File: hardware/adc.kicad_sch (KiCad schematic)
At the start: 6 parts, among them U2 AD8603

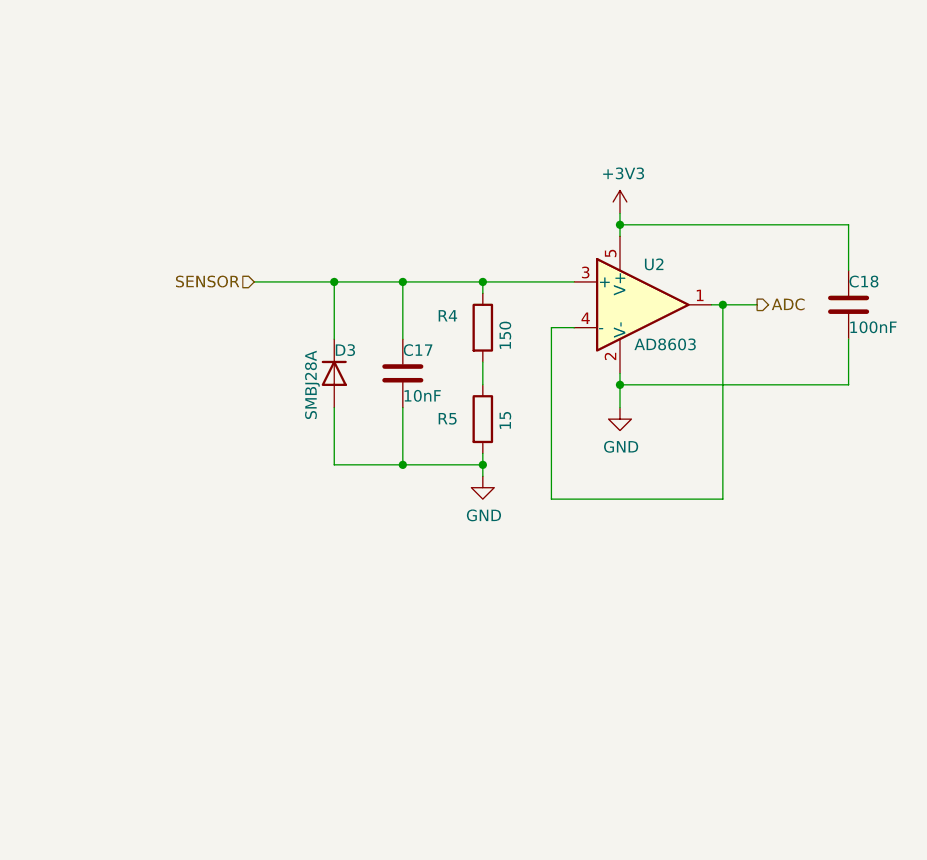
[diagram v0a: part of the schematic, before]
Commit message: MCU BOOT0 mistake fixed
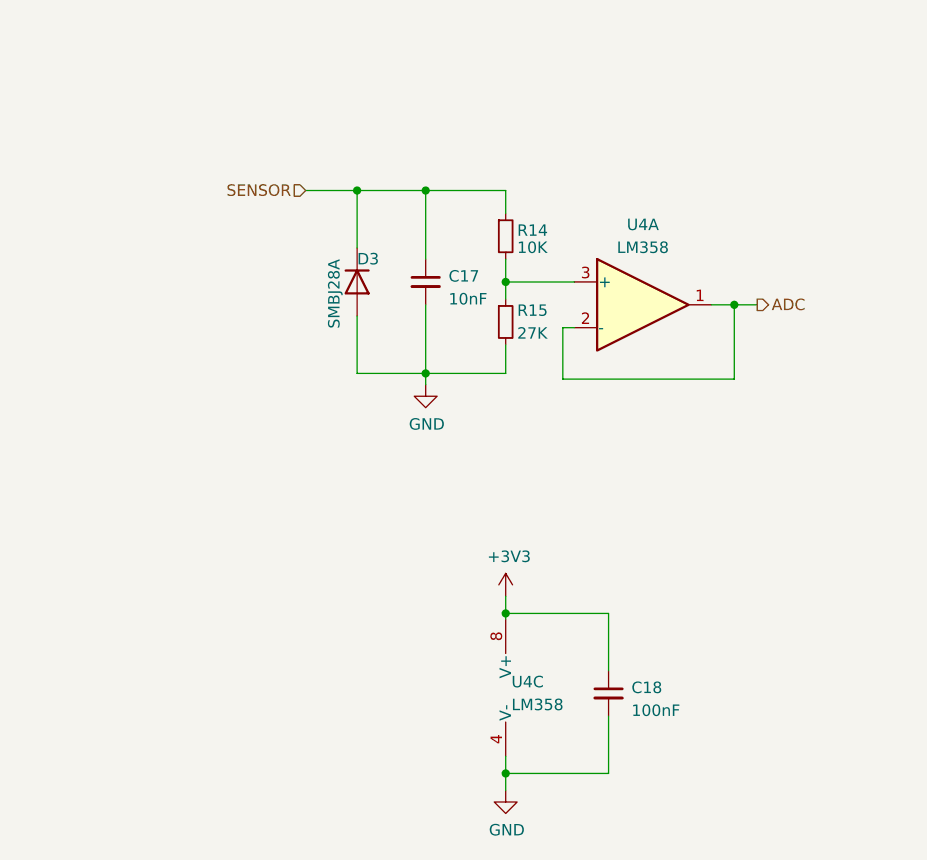
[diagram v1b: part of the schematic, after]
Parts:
- removed C17: 10nF, Capacitor_SMD:C_0603_1608Metric, symbol Device:C
- removed C18: 100nF, Capacitor_SMD:C_0603_1608Metric, symbol Device:C
- removed R4: 150, Resistor_SMD:R_0603_1608Metric, symbol Device:R
- removed R5: 15, Resistor_SMD:R_0603_1608Metric, symbol Device:R
- removed U2: AD8603, Package_TO_SOT_SMD:TSOT-23-5, symbol Amplifier_Operational:AD8603
- added C17: 10nF, Capacitor_SMD:C_0603_1608Metric, symbol Device:C_Small
- added C18: 100nF, Capacitor_SMD:C_0603_1608Metric, symbol Device:C_Small
- added R14: 10K, Resistor_SMD:R_0603_1608Metric, symbol Device:R_Small
- added R15: 27K, Resistor_SMD:R_0603_1608Metric, symbol Device:R_Small
- added U4: LM358, Damlama:SOIC127P599X175-8N, symbol Amplifier_Operational:LM358
- D3: Digikey SMBJ28ALFCT-ND -> (none); DigikeyPN (none) -> SMBJ28ALFDKR-ND
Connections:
- net +3V3: now also C18.1, U4.8 (V+)
- net ADC: now also U4.1, U4.2 (-)
- net GND: now also C17.2, C18.2, R15.2, U4.4 (V-)
- net SENSOR: now also C17.1, R14.1
- new net: R14.2, R15.1, U4.3 (+)
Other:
- moved on the sheet: D3
